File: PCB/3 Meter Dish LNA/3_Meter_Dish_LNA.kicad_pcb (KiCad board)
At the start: 2 copper layers, 86.4 x 45.7 mm, 24 parts, among them J1 Conn_Coaxial, J2 Conn_Coaxial, J3 Conn_Coaxial, U1 PMA2-63LN+, U2 PMA2-63LN+, U3 YAT-1A+, U4 L7805, U5 L7805

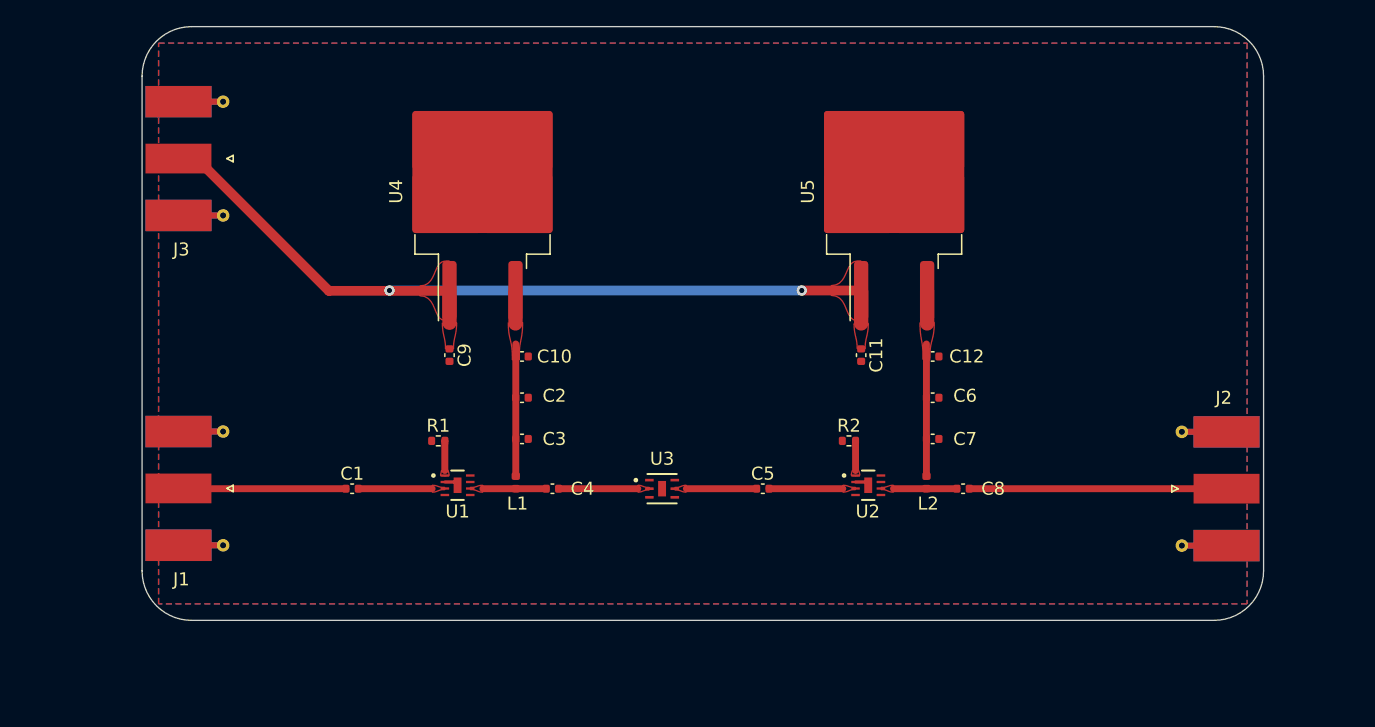
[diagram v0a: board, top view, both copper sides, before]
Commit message: PTH vias and mounting holes added
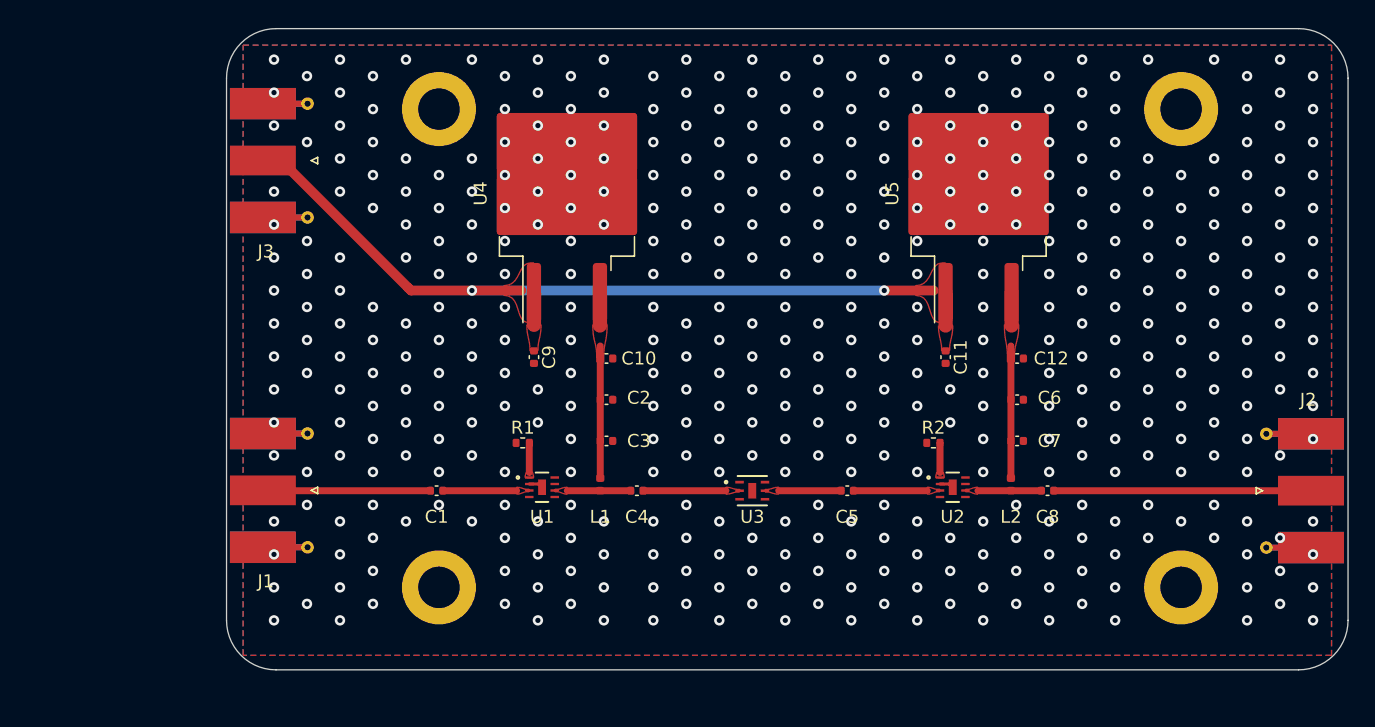
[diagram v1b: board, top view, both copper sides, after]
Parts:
- added REF**: MountingHole_3.2mm_M3_ISO7380_Pad, MountingHole:MountingHole_3.2mm_M3_ISO7380_Pad, F.Cu at (181.6, 78.7)
- added REF**: MountingHole_3.2mm_M3_ISO7380_Pad, MountingHole:MountingHole_3.2mm_M3_ISO7380_Pad, F.Cu at (124.5, 115.6)
- added REF**: MountingHole_3.2mm_M3_ISO7380_Pad, MountingHole:MountingHole_3.2mm_M3_ISO7380_Pad, F.Cu at (124.5, 78.7)
- added REF**: MountingHole_3.2mm_M3_ISO7380_Pad, MountingHole:MountingHole_3.2mm_M3_ISO7380_Pad, F.Cu at (181.6, 115.6)
- moved U3 6.95 mm to (148.6, 108.1)
- moved C12 6.51 mm to (169.0, 97.9)
- moved C6 6.51 mm to (169.0, 101.1)
- moved C7 6.51 mm to (169.0, 104.3)
- moved C1 6.51 mm to (124.3, 108.1)
- moved C9 6.51 mm to (131.8, 97.8)
- moved R1 6.51 mm to (130.9, 104.4)
- moved U4 6.51 mm to (134.3, 85.2)
- moved C10 6.51 mm to (137.4, 97.9)
- moved C11 6.51 mm to (163.5, 97.8)
- moved C2 6.51 mm to (137.4, 101.1)
- moved C3 6.51 mm to (137.4, 104.3)
- moved C4 6.51 mm to (139.7, 108.1)
- moved C5 6.51 mm to (155.9, 108.1)
- moved C8 6.51 mm to (171.3, 108.1)
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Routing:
- net Vin: track 66.4 -> 64.6 mm
- net /LNA Biasing1/LNA-IN: track 5.41 -> 4.80 mm
- net GND: vias 0 -> 466
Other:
- board size 86.4 x 45.7 mm -> 86.4 x 49.4 mm
- board text added: "7/6/2023"
- board text added: "A"
- board text added: "RF-DFS Gain Circuit"
- board text added: "Remy Nguyen"

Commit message: Relocated PTH vias, removed backups
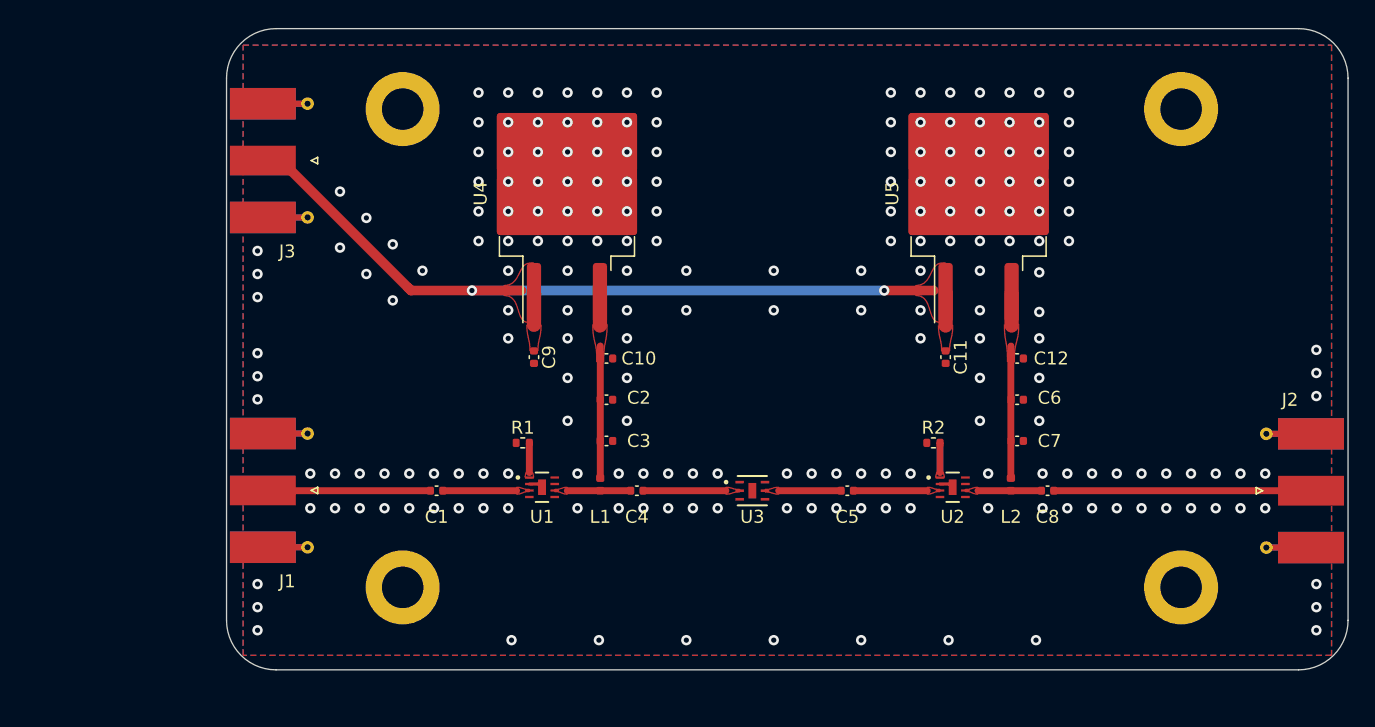
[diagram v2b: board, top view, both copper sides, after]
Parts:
- moved REF** 2.79 mm to (121.7, 115.6)
- moved REF** 2.79 mm to (121.7, 78.7)
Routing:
- net GND: vias 466 -> 209

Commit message: --no-edit
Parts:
- added G***: LOGO, Imports:nraoLogo12mm, F.Cu at (166.2, 93.3)
- moved C1 15.6 mm to (108.9, 110.5)
- moved C11 15.6 mm to (148.1, 100.2)
- moved C12 15.6 mm to (153.6, 100.3)
- moved C4 15.6 mm to (124.3, 110.5)
- moved C5 15.6 mm to (140.5, 110.5)
- moved C7 15.6 mm to (153.6, 106.7)
- moved C8 15.6 mm to (155.9, 110.5)
- moved C9 15.6 mm to (116.4, 100.2)
- moved J2 15.6 mm to (174.5, 110.5)
- moved L1 15.6 mm to (121.5, 110.0)
- moved REF** 15.6 mm to (166.2, 81.1)
- moved U3 15.6 mm to (133.2, 110.5)
- moved U4 15.6 mm to (118.9, 87.6)
- moved C6 15.6 mm to (153.6, 103.5)
- moved R1 15.6 mm to (115.5, 106.8)
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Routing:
- net Vdd2: track 12.7 -> 10.2 mm
- net Vdd1: track 12.7 -> 10.2 mm
- net GND: vias 209 -> 259
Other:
- board text added: "Designed By: Remy Nguyen"
- board text added: "RF-DFS"
